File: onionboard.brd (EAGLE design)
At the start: 100 x 90.2 mm, 173 parts, among them IC1 IR4427S, IC2 IR4427S, J1 22-27-2041-04, Q1 FDD4141TO252, Q2 FDD4141TO252, Q3 FDD4141TO252, Q4 FDD4141TO252, Q5 FDD4141TO252, Q6 FDD4141TO252, X1 5569-8, X2 5569-6, X3 5569-6

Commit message: Cleaned up and rearranged the schematic. Moved two ground vias on monitor schottkys
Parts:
- renumbered LSP11 to VR1-, LSP14 to VR1+, LSP15 to VR2+, LSP16 to VR2-, PAD1 to HALL1, PAD10 to IGN2, PAD11 to IGN3, PAD12 to IGN4, PAD2 to HALL2, PAD25 to AD3, PAD26 to AD4, PAD31 to BRV, PAD33 to SW1, PAD34 to SW2, PAD37 to ACCMON, PAD38 to INJMON, PAD9 to IGN1
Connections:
- net 12VOLT renamed +12V
- net 5VOLT renamed +5V
- net GND2 renamed GND
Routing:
- net GND: track 234.8 -> 232.7 mm, vias 50 -> 52
- net +5V: track 356.6 -> 358.6 mm

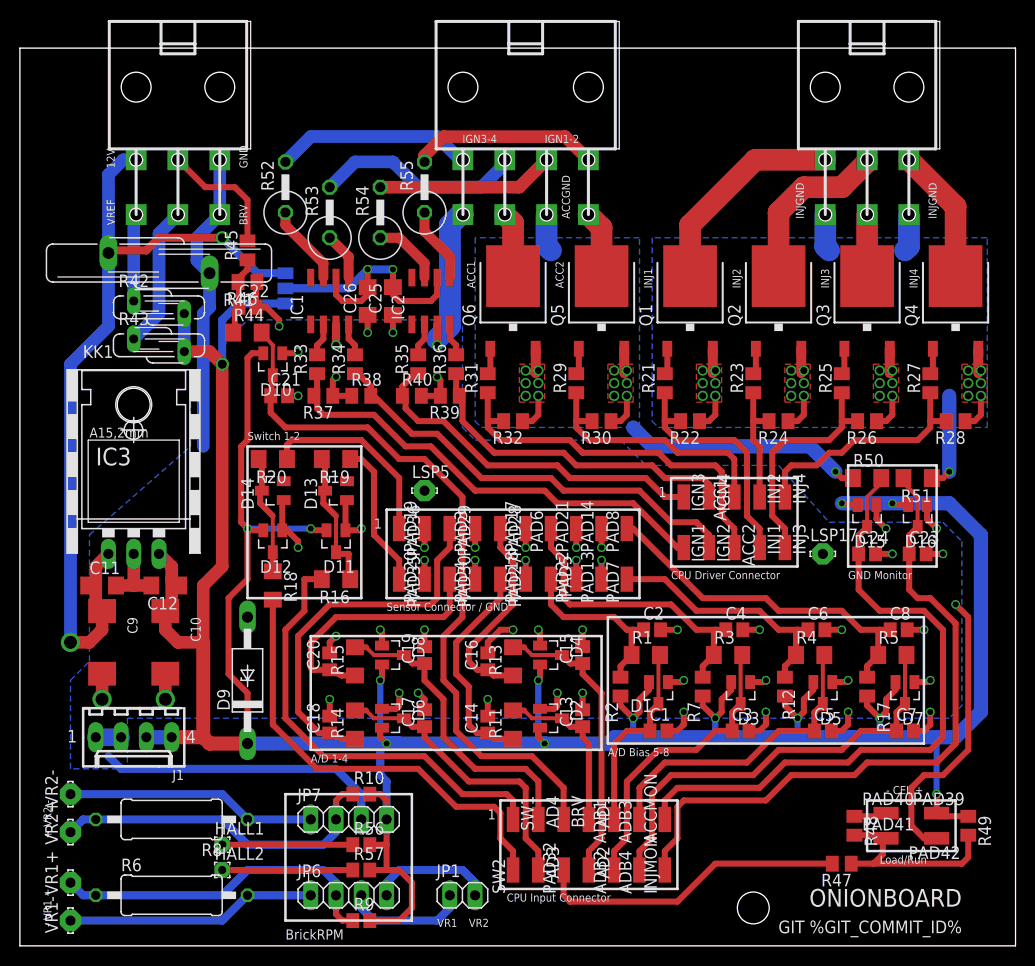
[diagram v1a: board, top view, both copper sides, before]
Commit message: Even more schematic refactor and added values to components. Added silkscreen for molex connectors
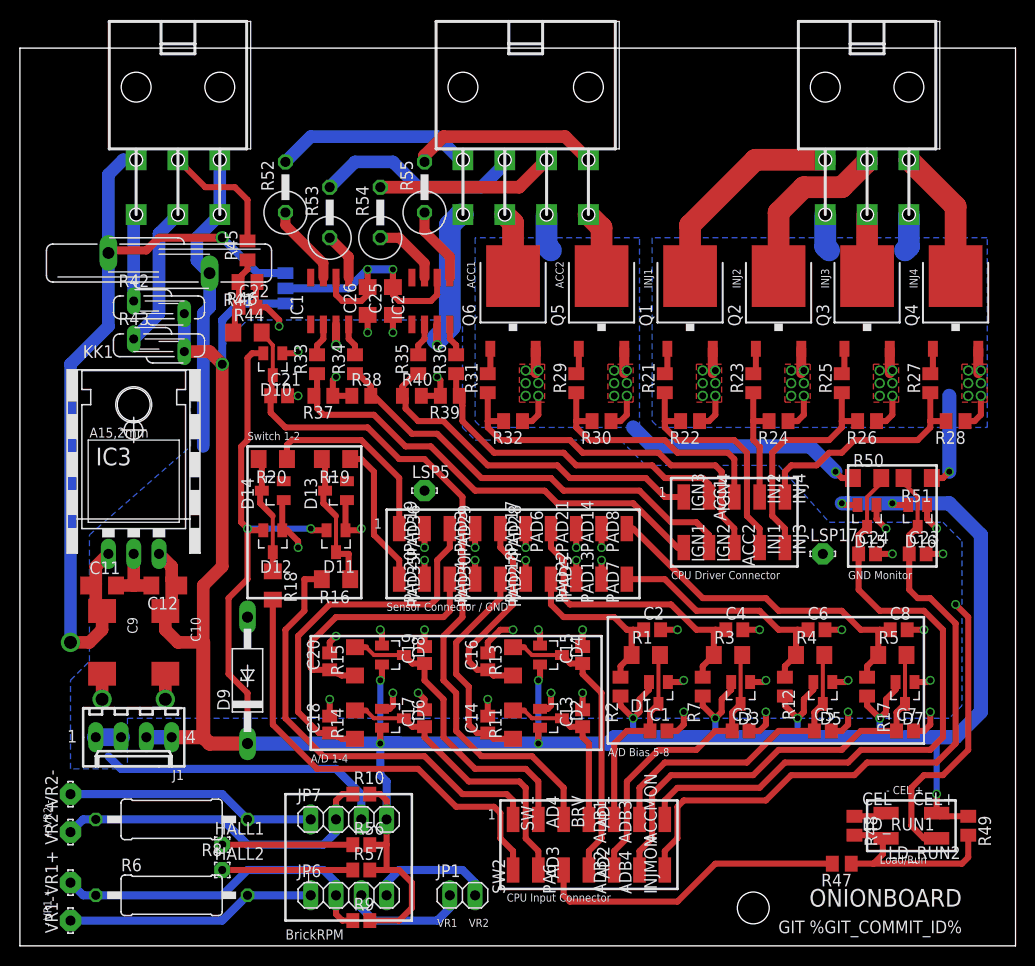
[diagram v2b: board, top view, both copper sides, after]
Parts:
- C1, C25, C26, C3, C5, C7: value (none) -> 1uF
- C10: value (none) -> 47uF
- C11, C12, C14, C16, C18, C2, C20, C22, C4, C6, C8: value (none) -> 0.1uF
- C13, C15, C17, C19, C21: value (none) -> 0.22uF
- C23, C24: value (none) -> 15nF
- C9: value (none) -> 10uF
- D13, D14: value (none) -> 4.7V
- D9: value (none) -> 5.1V
- IC1, IC2: value IR4427S -> TC442xA
- IC3: value (none) -> LM2940
- Q1, Q2, Q3, Q4, Q5, Q6: value FDD4141TO252 -> VND14NV04
- R1, R11, R13, R14, R15, R3, R4, R44, R5, R50, R51: value (none) -> 470R
- R10, R16, R18, R19, R20, R21, R23, R25, R27, R29, R31, R33, R34, R35, R36, R46, R47, R48, R56, R57, R9: value (none) -> 1k
- R12, R17, R2, R7: value (none) -> 2.49k
- R22, R24, R26, R28, R30, R32, R37, R38, R39, R40: value (none) -> 100k
- R45: value (none) -> 3.9k
- R49: value (none) -> 2.4k
- R52, R53, R54, R55: value (none) -> 100R
- R6, R8: value (none) -> 5k
- renumbered PAD32 to PA6, PAD39 to CEL+, PAD40 to CEL-, PAD41 to LD_RUN1, PAD42 to LD_RUN2
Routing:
- net GND: track 232.7 -> 231.5 mm

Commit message: Changed VDR/MOV size from 20mm to 14mm. Moved powersupply section a bit lower to fit the heatsink properly
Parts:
- R41: value S20K20 -> S14K11; device varistor:S20K20 -> varistor:S14K11
- moved R41 1.80 mm to (12.7, 69.8)
- moved C11 1.27 mm to (8.26, 34.9)
- moved C12 1.27 mm to (14.6, 34.9)
- moved IC3 1.27 mm to (11.4, 41.9)
- moved KK1 1.27 mm to (11.4, 47.6)
- moved C10 1.27 mm to (14.6, 29.2)
- moved C9 1.27 mm to (8.26, 29.2)
- moved J1 1.27 mm to (11.4, 19.7)
- moved R42 1.27 mm to (14.0, 65.4)
- moved R43 1.27 mm to (14.0, 61.6)
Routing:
- net +5V: track 358.7 -> 360.4 mm
- net N$52: track 8.78 -> 7.51 mm
- net N$51: track 14.3 -> 13.1 mm
- net +12V: track 84.7 -> 85.5 mm
- net GND: track 231.5 -> 232.0 mm
